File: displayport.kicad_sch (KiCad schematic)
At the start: 56 parts, among them U1 MIMX8MM6DVTLZAA, U35 LP5912-1.2DRV, U36 SN65DSI86, U37 TPD4E02B04, U38 TPD4E02B04, U39 TPD4E02B04, U40 Connector_Displayport_Source, X1 26Mhz

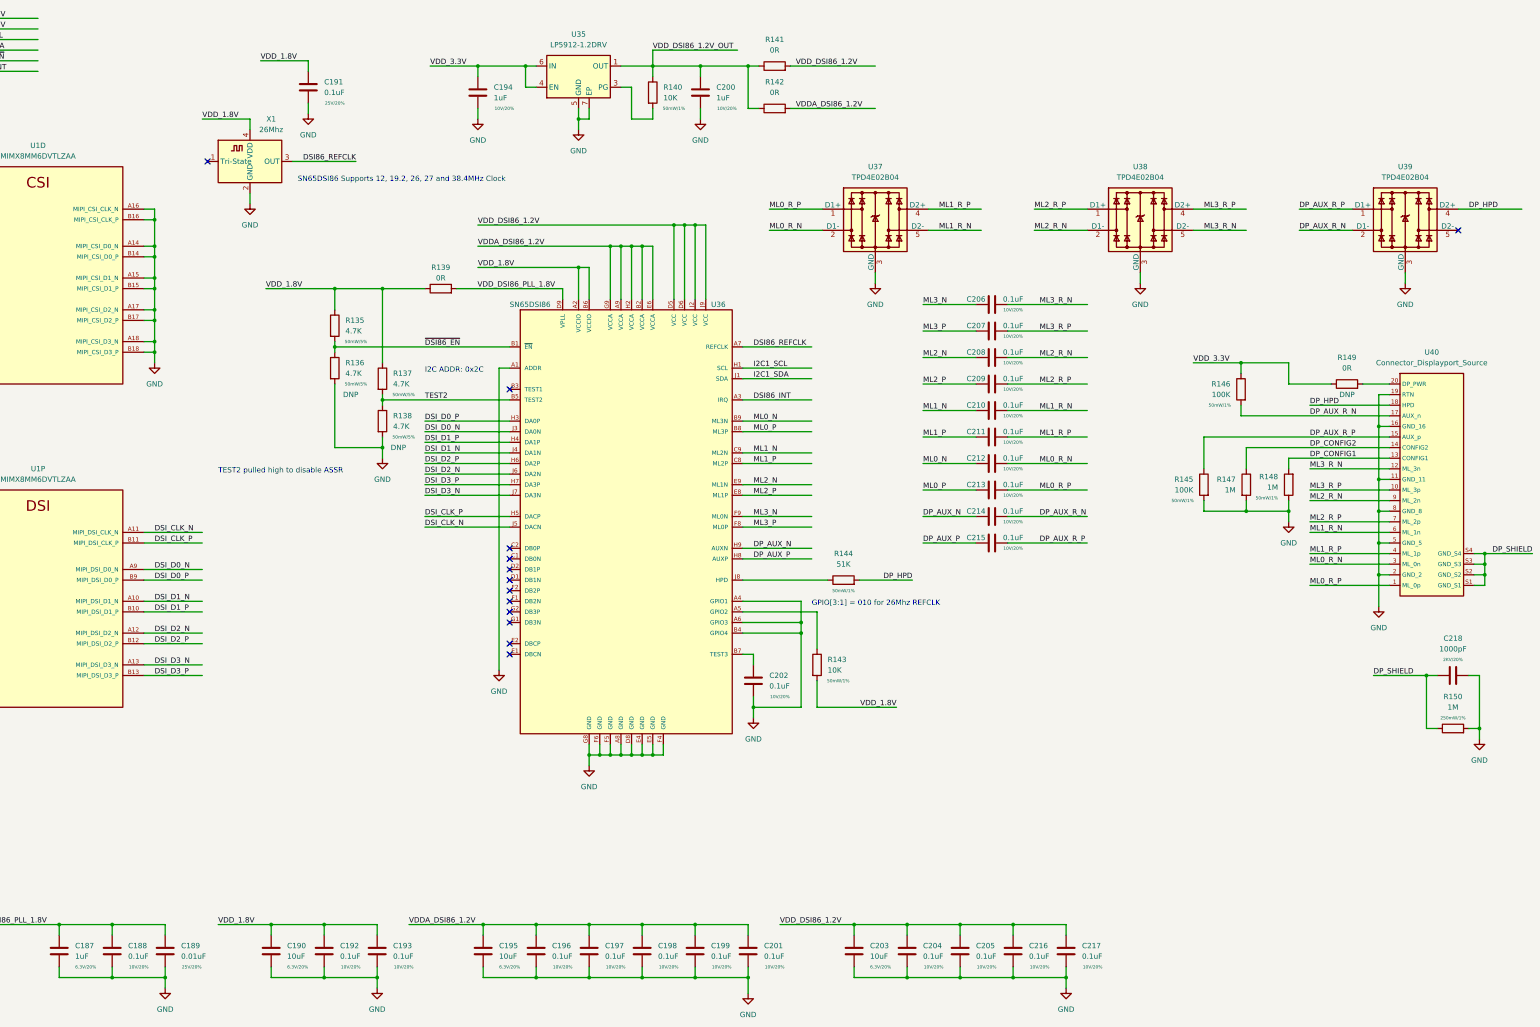
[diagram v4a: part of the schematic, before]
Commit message: ddr length matching work, misc cleanup
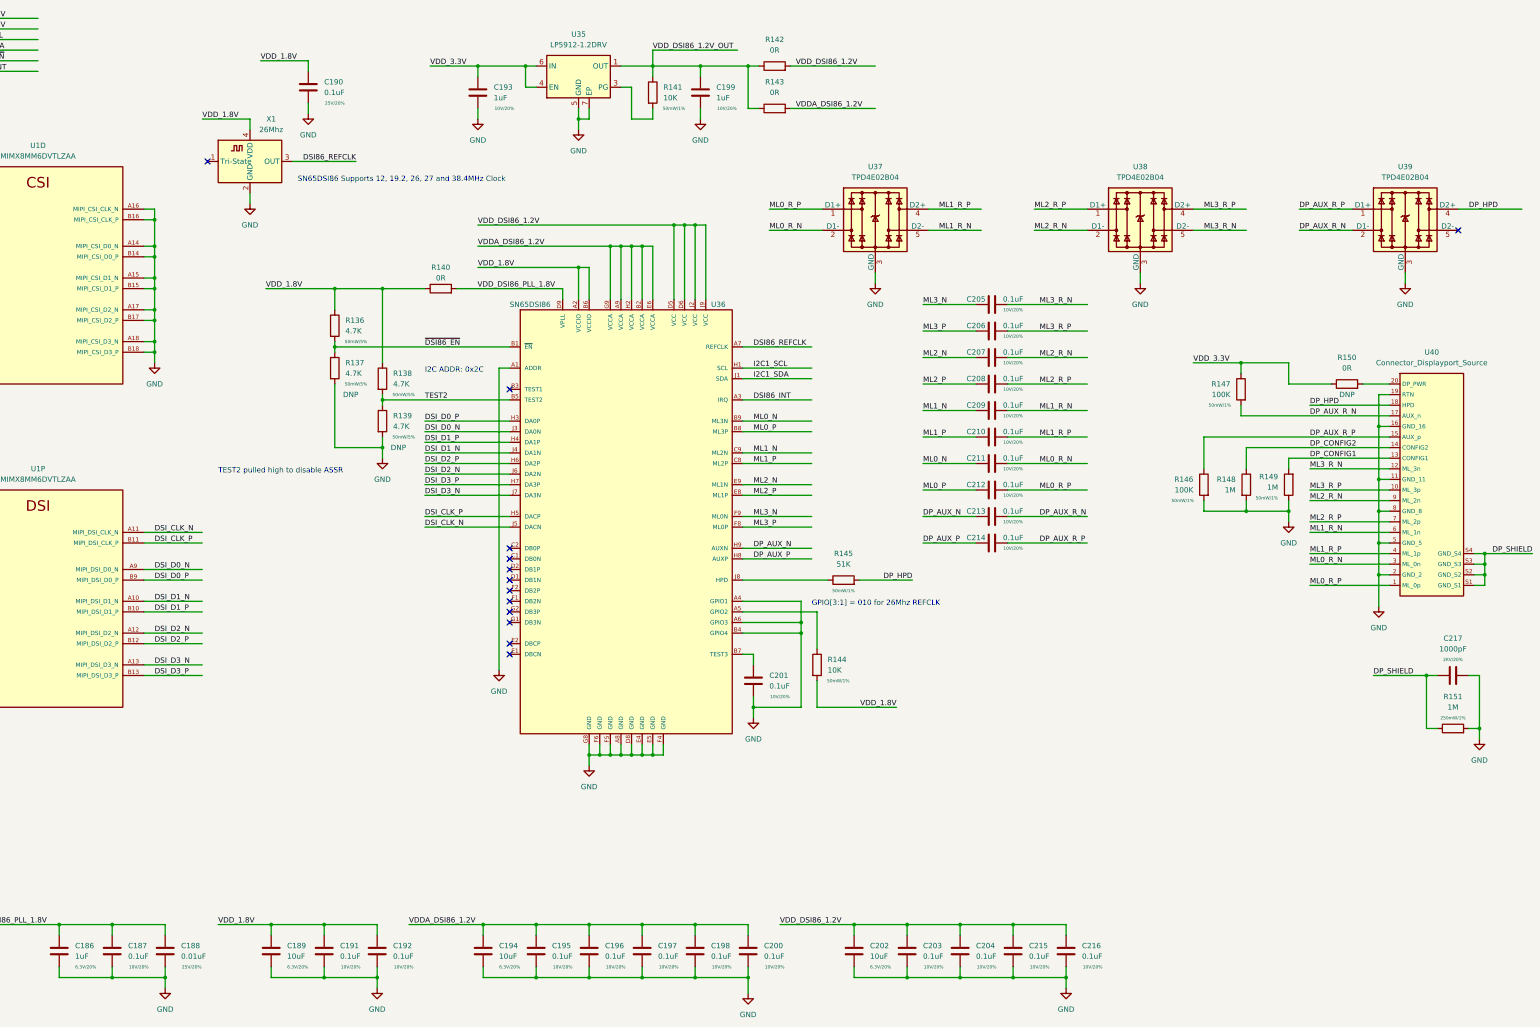
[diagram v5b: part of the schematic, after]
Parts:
- renumbered C187 to C186, C188 to C187, C189 to C188, C190 to C189, C191 to C190, C192 to C191, C193 to C192, C194 to C193, C195 to C194, C196 to C195, C197 to C196, C198 to C197, C199 to C198, C200 to C199, C201 to C200, C202 to C201, C203 to C202, C204 to C203, C205 to C204, C206 to C205, C207 to C206, C208 to C207, C209 to C208, C210 to C209, C211 to C210, C212 to C211, C213 to C212, C214 to C213, C215 to C214, C216 to C215, C217 to C216, C218 to C217, R135 to R136, R136 to R137, R137 to R138, R138 to R139, R139 to R140, R140 to R141, R141 to R142, R142 to R143, R143 to R144, R144 to R145, R145 to R146, R146 to R147, R147 to R148, R148 to R149, R149 to R150, R150 to R151

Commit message: misc cleanup, change from usb mux to dual uart
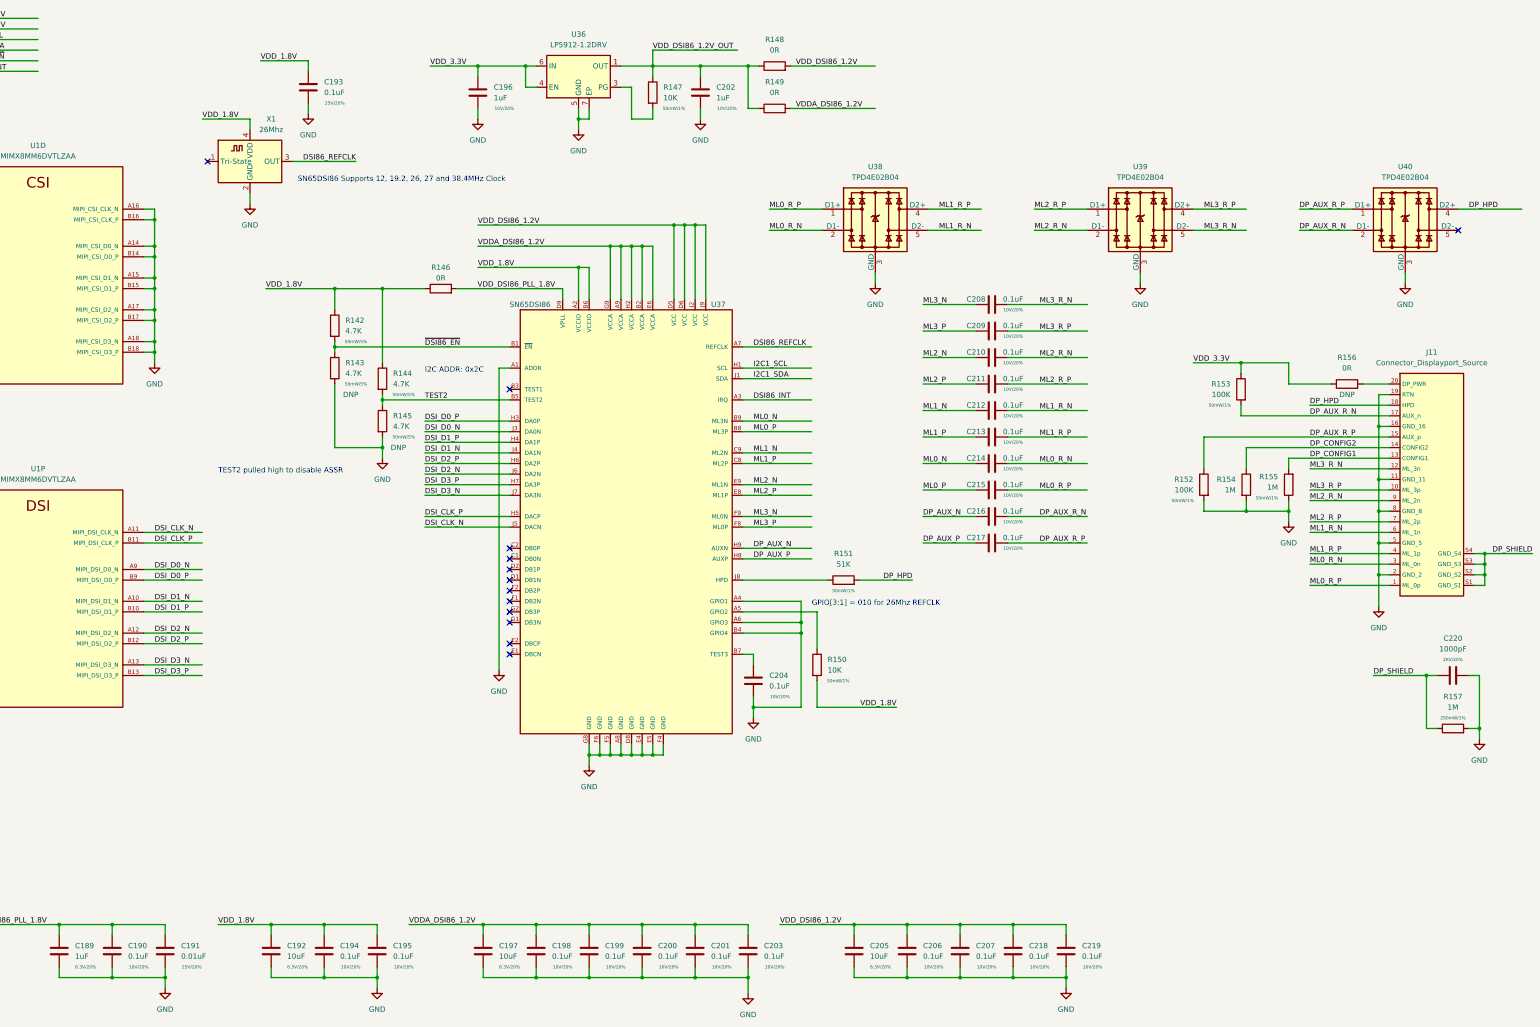
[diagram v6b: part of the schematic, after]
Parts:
- renumbered C186 to C189, C187 to C190, C188 to C191, C189 to C192, C190 to C193, C191 to C194, C192 to C195, C193 to C196, C194 to C197, C195 to C198, C196 to C199, C197 to C200, C198 to C201, C199 to C202, C200 to C203, C201 to C204, C202 to C205, C203 to C206, C204 to C207, C205 to C208, C206 to C209, C207 to C210, C208 to C211, C209 to C212, C210 to C213, C211 to C214, C212 to C215, C213 to C216, C214 to C217, C215 to C218, C216 to C219, C217 to C220, U40 to J11, R136 to R142, R137 to R143, R138 to R144, R139 to R145, R140 to R146, R141 to R147, R142 to R148, R143 to R149, R144 to R150, R145 to R151, R146 to R152, R147 to R153, R148 to R154, R149 to R155, R150 to R156, R151 to R157, U35 to U36, U36 to U37, U37 to U38, U38 to U39, U39 to U40

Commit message: Rev 1
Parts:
- renumbered R142 to R141, R143 to R142, R144 to R143, R145 to R144, R146 to R145, R147 to R146, R148 to R147, R149 to R148, R150 to R149, R151 to R150, R152 to R151, R153 to R152, R154 to R153, R155 to R154, R156 to R155, R157 to R156
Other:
- company: (none) -> Q-LAB
- title: (none) -> QSBC

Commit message: misc changes for rev1
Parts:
- C220: MPN C1210C102KGRAC7800 -> C1210C102KGRACTU
- J11: MPN 472720001 -> 47272-0001
- R142, R144, R155: now left out of the parts list
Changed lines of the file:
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@@
       (effects (font (size 1.27 1.27)) hide)
     )
-    (property "MPN" "472720001" (id 4) (at 379.73 130.81 0)
+    (property "MPN" "47272-0001" (id 4) (at 379.73 130.81 0)
       (effects (font (size 1.27 1.27)) hide)
     )
@@
   )
   (symbol (lib_id "Device:R") (at 116.84 102.87 0) (unit 1)
-    (in_bom yes) (on_board yes)
+    (in_bom no) (on_board yes)
     (property "Reference" "R142" (id 0) (at 119.38 101.5999 0)
       (effects (font (size 1.27 1.27)) (justify left))
@@
   )
   (symbol (lib_id "Device:R") (at 359.41 106.68 90) (unit 1)
-    (in_bom yes) (on_board yes)
+    (in_bom no) (on_board yes)
     (property "Reference" "R155" (id 0) (at 359.41 100.33 90))
     (property "Value" "0R" (id 1) (at 359.41 102.87 90))
@@
   )
   (symbol (lib_id "Device:R") (at 128.27 115.57 0) (unit 1)
-    (in_bom yes) (on_board yes)
+    (in_bom no) (on_board yes)
     (property "Reference" "R144" (id 0) (at 130.81 114.2999 0)
       (effects (font (size 1.27 1.27)) (justify left))
@@
       (effects (font (size 0.762 0.762)))
     )
-    (property "MPN" "C1210C102KGRAC7800" (id 5) (at 384.81 176.53 0)
-      (effects (font (size 1.27 1.27)) hide)
-    )
+    (property "MPN" "C1210C102KGRACTU" (id 5) (at 384.81 176.53 0)
+      (effects (font (size 1.27 1.27)) hide)
+    )
